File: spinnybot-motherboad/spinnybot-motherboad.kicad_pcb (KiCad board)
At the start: 2 copper layers, 109.4 x 86 mm, 83 parts, among them J1 ENCODER 1, J10 ESC_POS, J11 POWER SW2, J12 LEDSTRIP3, J13 LEDSTRIP2, J14 LEDSTRIP3, J15 BAT_GND, J16 ESC_GND, J2 LEDSTRIP1, J3 LEDSTRIP1, J4 LEDSTRIP2, J5 ENCODER 2, J6 ENCODER 3, J7 CONN_SM10B-SRSS-TB_JST, J8 BAT_POS, J9 POWER SW1, Q1 SISA96DN, Q2 SISA96DN, Q3 BC846, Q4 Q_NMOS_DGS, U1 LM1117-3.3, U10 MMA3221KEG, U11 ADS122U04IPWR, U12 ADS122U04IPWR, U2 XBP9B-DMWTB002, U3 MC14504BDR2G, U4 ICM-20649, U5 ESP32-DEVKITC-32D, U6 TSOP6_SOT457_NEX, U7 SN74AHCT541DW, U8 SN74LVC1G18DBVR, U9 MMA3221KEG

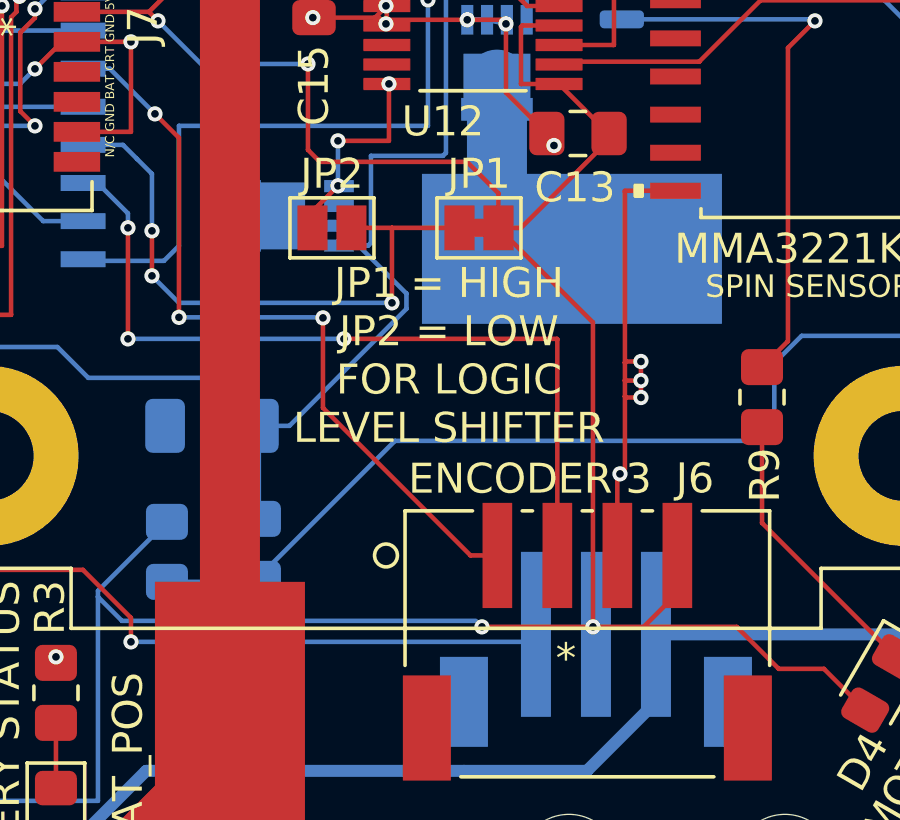
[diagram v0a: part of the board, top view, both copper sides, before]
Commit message: fix LEDSTRIP_GND on the FET not being connected
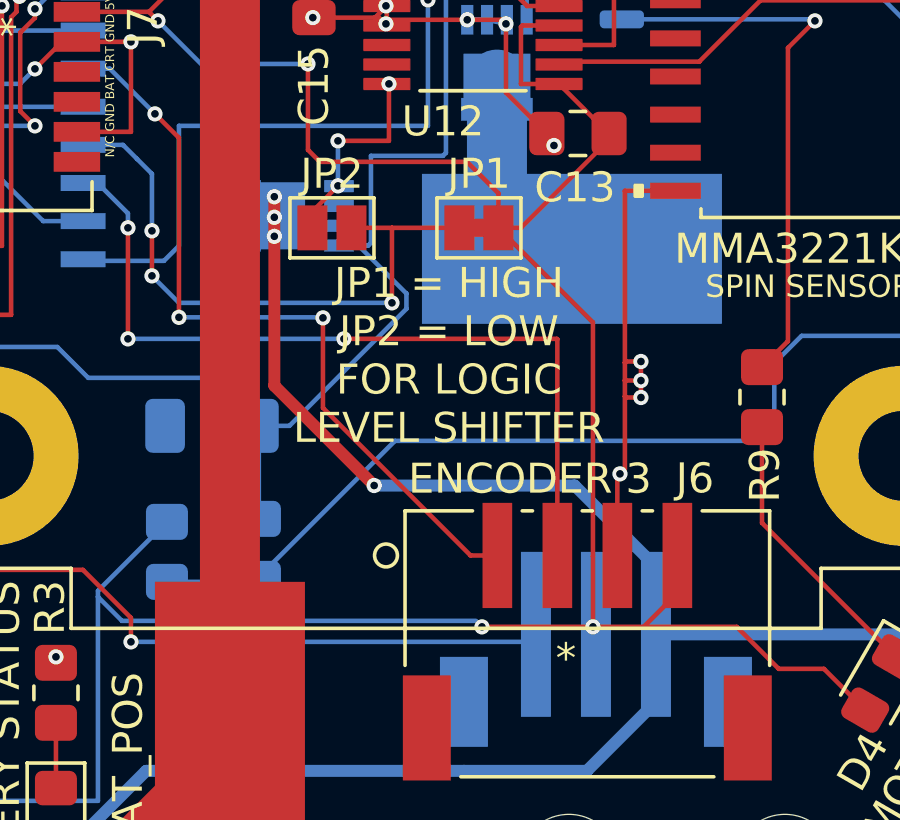
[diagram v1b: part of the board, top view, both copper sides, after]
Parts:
- J7: value CONN_SM10B-SRSS-TB_JST -> SM10B-SRSS-TB
- U6: value TSOP6_SOT457_NEX -> 74LVC1G157GV_125
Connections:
- Q1 pad 5: /LEDSTRIP_GROUND -> /LEDSTRIP_GND
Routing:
- net /LEDSTRIP_GND: track 171.5 -> 195.2 mm, vias 6 -> 10

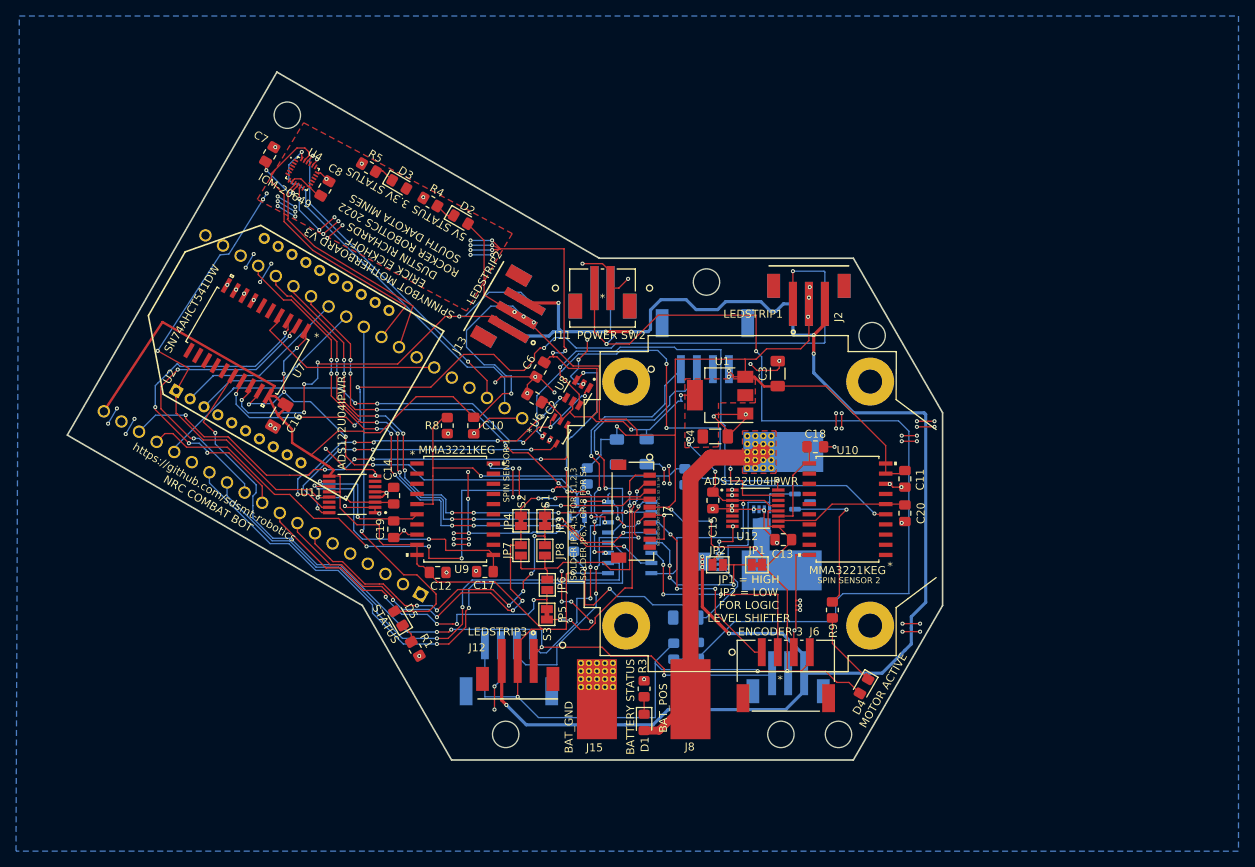
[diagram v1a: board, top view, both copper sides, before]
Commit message: tweaks to routing to make the ground plane more connected, add a top copper ground pour. move ESC FET.
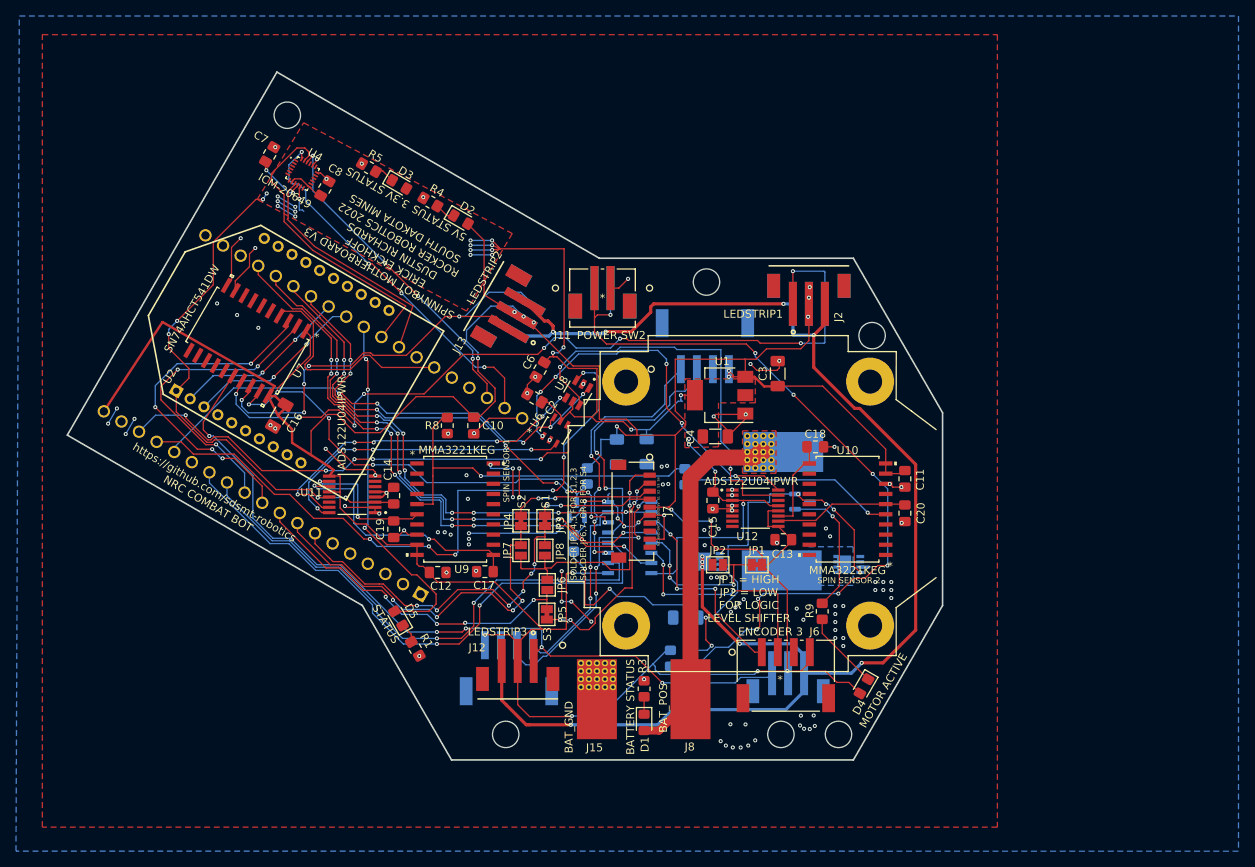
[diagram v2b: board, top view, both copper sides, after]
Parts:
- moved Q2 12.2 mm to (185.8, 125.7), turned to 180 degrees
- moved R7 1.48 mm to (165.9, 137.4)
- moved R9 1.28 mm to (182.5, 131.5)
- moved R6 0.98 mm to (163.5, 137.4)
- renumbered REF** to A1
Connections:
- net Net-(J11-Pad2) renamed /Power/POWER_SW_IN
- U7 pad 5: unconnected-(U7-Pad5) -> GND
- U7 pad 6: unconnected-(U7-Pad6) -> GND
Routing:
- net GND: track 235.1 -> 135.3 mm, vias 116 -> 118
- net /Power/POWER_SW_IN: track 122.5 -> 100.3 mm, vias 2 -> 8
- net /POWER_ON: track 56.4 -> 74.2 mm, vias 2 -> 8
- net /LEDSTRIP_GND: track 195.2 -> 184.3 mm
- net +5V: track 410.3 -> 400.8 mm, vias 16 -> 17
- net /Power/ESC_GND: track 6.68 -> 15.5 mm
- net /IMU and Accelerometers/ADC2_RX: track 54.2 -> 48.9 mm, vias 4 -> 6
- net /MCU and Buffers/LEDSTRIP3_DATA_3V3: track 24.8 -> 28.7 mm
- net /ADC_TX: track 86.6 -> 83.6 mm
- net /LEDSTRIP1_DATA_5V: track 105.1 -> 103.0 mm, vias 6 -> 8
- net /MCU and Buffers/ENC_2A_3V3: track 56.1 -> 58.0 mm
- net /MCU and Buffers/ENC_2B_3V3: track 65.4 -> 67.0 mm
- net Net-(Q4-Pad1): track 18.7 -> 17.2 mm
- net /ENC_2B_5V: track 35.9 -> 34.5 mm
- net Net-(C17-Pad1): track 33.7 -> 32.4 mm
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- added copper zone on B.Cu, net /Power/ESC_GND
- added copper zone on F.Cu, net GND

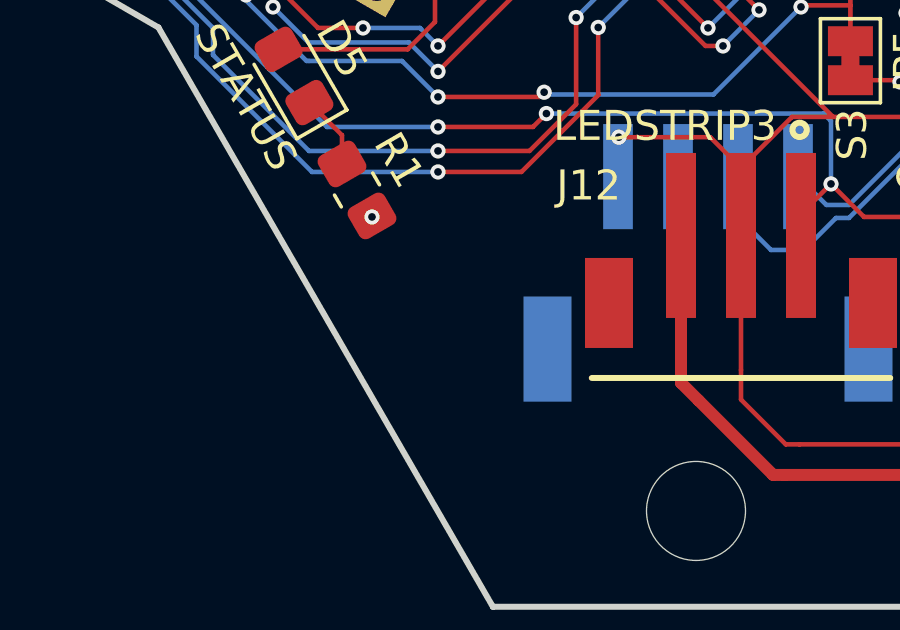
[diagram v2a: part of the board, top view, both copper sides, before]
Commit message: add a couple ground test points
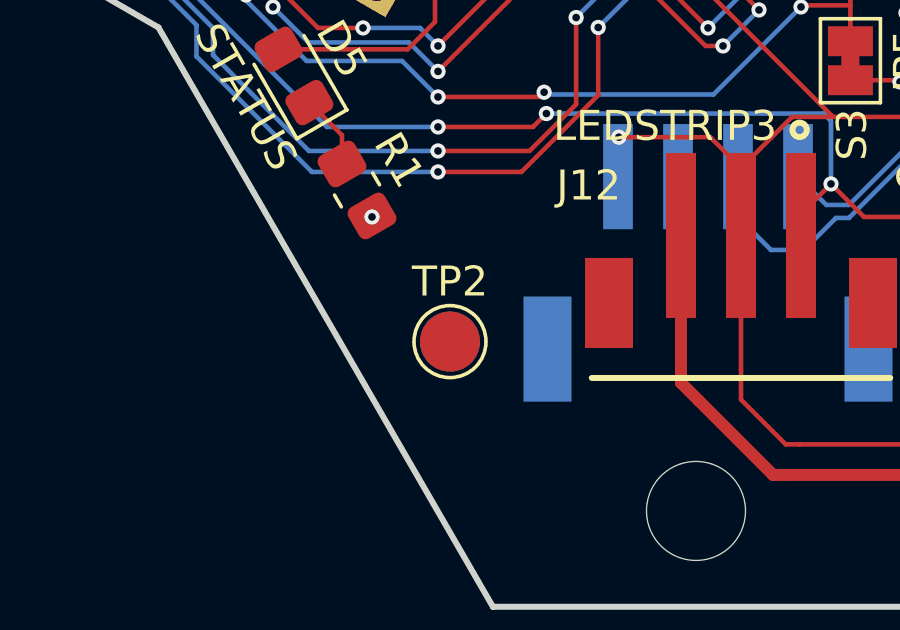
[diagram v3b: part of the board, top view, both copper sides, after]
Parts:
- added TP1: TestPoint, TestPoint:TestPoint_Pad_D2.0mm, B.Cu at (134.7, 141.3)
- added TP2: TestPoint, TestPoint:TestPoint_Pad_D2.0mm, F.Cu at (134.7, 141.3)
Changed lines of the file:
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@@
     )
+  )
+  (footprint "TestPoint:TestPoint_Pad_D2.0mm" (layer "F.Cu")
+    (at 134.7 141.255)
+    (descr "SMD pad as test Point, diameter 2.0mm")
+    (tags "test point SMD pad")
+    (property "Sheetfile" "power.kicad_sch")
+    (property "Sheetname" "Power")
+    (attr exclude_from_pos_files)
+    (fp_text reference "TP2" (at 0 -1.998) (layer "F.SilkS")
+      (effects (font (size 1 1) (thickness 0.15)))
+    )
+    (fp_text value "TestPoint" (at 0 2.05) (layer "F.Fab")
+      (effects (font (size 1 1) (thickness 0.15)))
+    )
+    (fp_text user "${REFERENCE}" (at 0 -2) (layer "F.Fab")
+      (effects (font (size 1 1) (thickness 0.15)))
+    )
+    (fp_circle (center 0 0) (end 0 1.2) (layer "F.SilkS") (width 0.12) (fill none))
+    (fp_circle (center 0 0) (end 1.5 0) (layer "F.CrtYd") (width 0.05) (fill none))
+    (pad "1" smd circle (at 0 0) (size 2 2) (layers "F.Cu" "F.Mask")
+      (net 5 "GND") (pinfunction "1") (pintype "passive"))
   )
   (footprint "Capacitor_SMD:C_0805_2012Metric_Pad1.18x1.45mm_HandSolder" (layer "F.Cu")
@@
     )
   )
+  (footprint "TestPoint:TestPoint_Pad_D2.0mm" (layer "B.Cu")
+    (at 134.7 141.255 180)
+    (descr "SMD pad as test Point, diameter 2.0mm")
+    (tags "test point SMD pad")
+    (property "Sheetfile" "power.kicad_sch")
+    (property "Sheetname" "Power")
+    (attr exclude_from_pos_files)
+    (fp_text reference "TP1" (at 0 1.998) (layer "B.SilkS")
+      (effects (font (size 1 1) (thickness 0.15)) (justify mirror))
+    )
+    (fp_text value "TestPoint" (at 0 -2.05) (layer "B.Fab")
+      (effects (font (size 1 1) (thickness 0.15)) (justify mirror))
+    )
+    (fp_text user "${REFERENCE}" (at 0 2) (layer "B.Fab")
+      (effects (font (size 1 1) (thickness 0.15)) (justify mirror))
+    )
+    (fp_circle (center 0 0) (end 0 -1.2) (layer "B.SilkS") (width 0.12) (fill none))
+    (fp_circle (center 0 0) (end 1.5 0) (layer "B.CrtYd") (width 0.05) (fill none))
+    (pad "1" smd circle (at 0 0 180) (size 2 2) (layers "B.Cu" "B.Mask")
+      (net 5 "GND") (pinfunction "1") (pintype "passive"))
+  )
   (footprint "B3B-PH-SM4:JST_B3B-PH-SM4-TB(LF)(SN)" (layer "B.Cu")

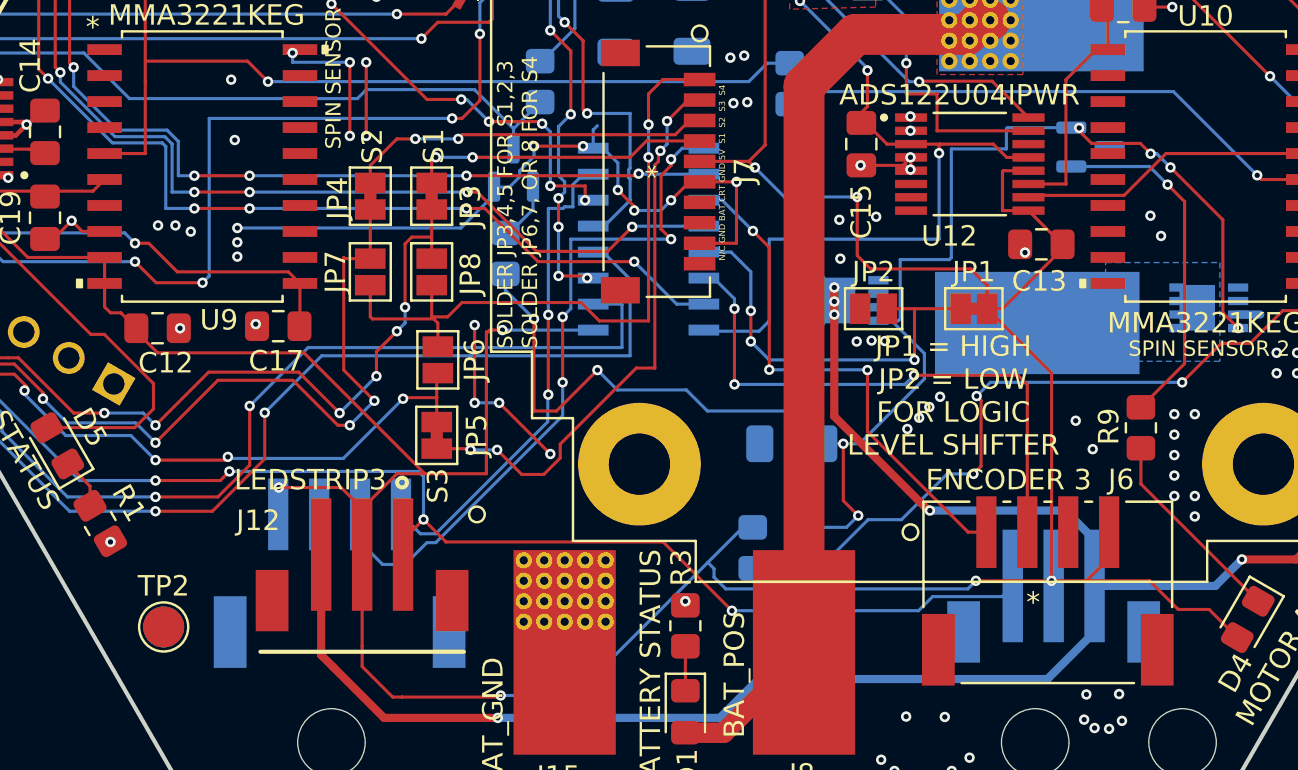
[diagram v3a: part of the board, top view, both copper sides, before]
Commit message: swap out motor active indicator FET for a BJT we already have
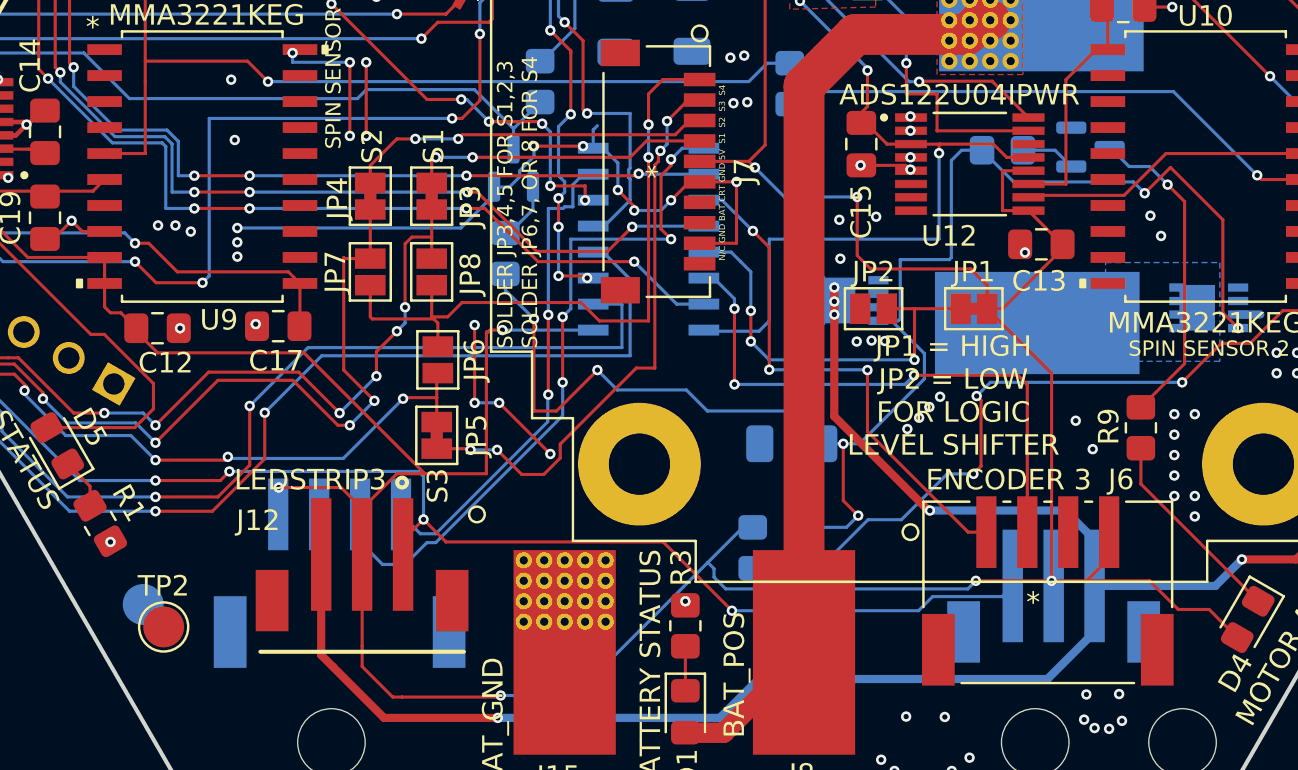
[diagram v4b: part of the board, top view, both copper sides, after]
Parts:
- added R10: 10K, Resistor_SMD:R_0805_2012Metric_Pad1.20x1.40mm_HandSolder, B.Cu at (175.7, 118.0)
- Q4: value Q_NMOS_DGS -> BC846
- moved TP1 1.49 mm to (133.7, 140.2)
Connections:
- Q4 pad 1: Net-(Q4-Pad1) -> Net-(R10-Pad2)
- Q4 pad 2: /POWER_ON -> GND
- Q4 pad 3: GND -> Net-(R9-Pad1)
- R9 pad 1: Net-(Q4-Pad1) -> Net-(R9-Pad1)
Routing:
- net Net-(Q4-Pad1): track 17.2 -> 0.00 mm, vias 1 -> 0
- net Net-(R9-Pad1): track 0.00 -> 15.7 mm, vias 0 -> 1
- net /Power/ESC_GND: track 15.5 -> 12.0 mm
- net Net-(R10-Pad2): track 0.00 -> 2.69 mm
- net GND: track 135.3 -> 133.4 mm
- net /POWER_ON: track 74.2 -> 73.8 mm, vias 8 -> 6
